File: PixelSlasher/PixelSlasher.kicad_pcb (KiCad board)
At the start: 2 copper layers, 52.8 x 123.6 mm, 16 parts, among them J1 VGA Input, Q1 BC337, Q2 BC337, Q3 BC337, U1 LM393, U2 LM393

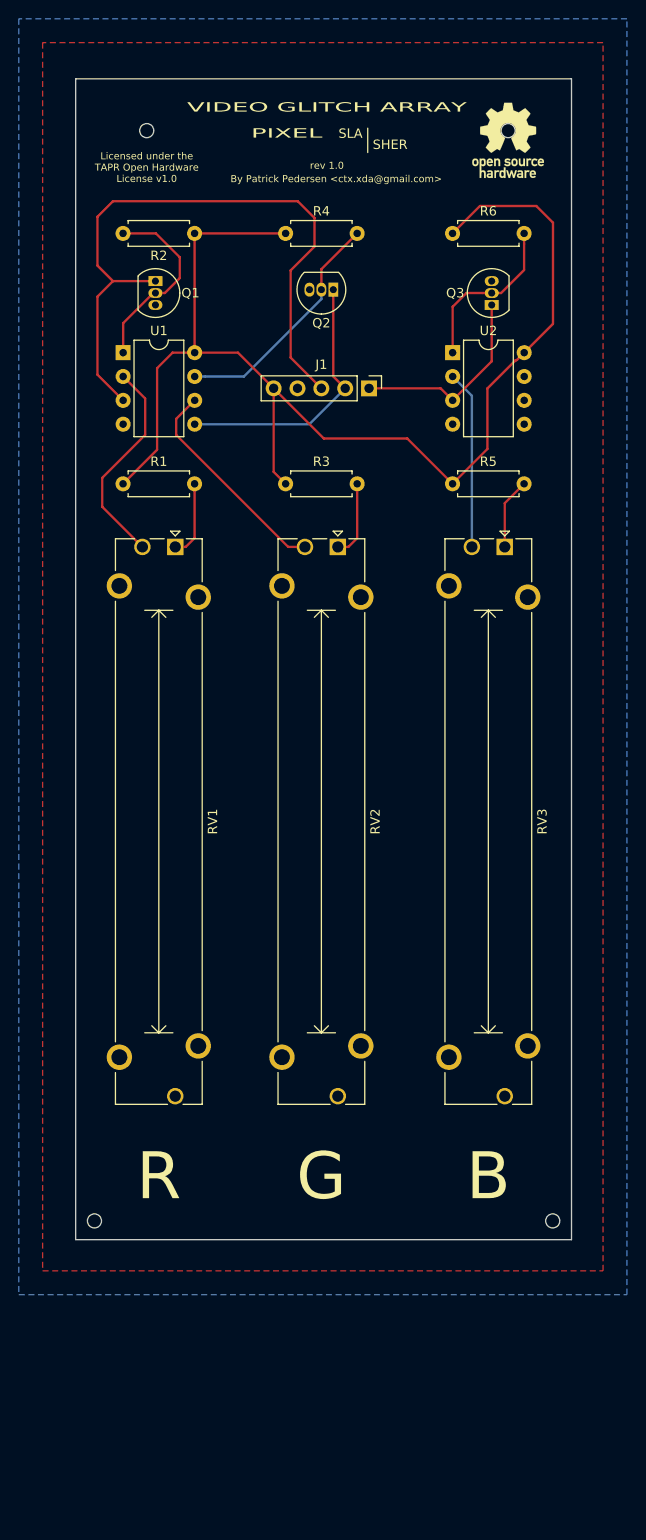
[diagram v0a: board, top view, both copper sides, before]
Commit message: Pixel Slasher: Rev 1.1: Inverted direction of slide pots
The previous configuration was counter-intuitive as we were decreasing
the number of artifacts as the slider went up.

Signed-off-by: Patrick Pedersen <ctx.xda@gmail.com>
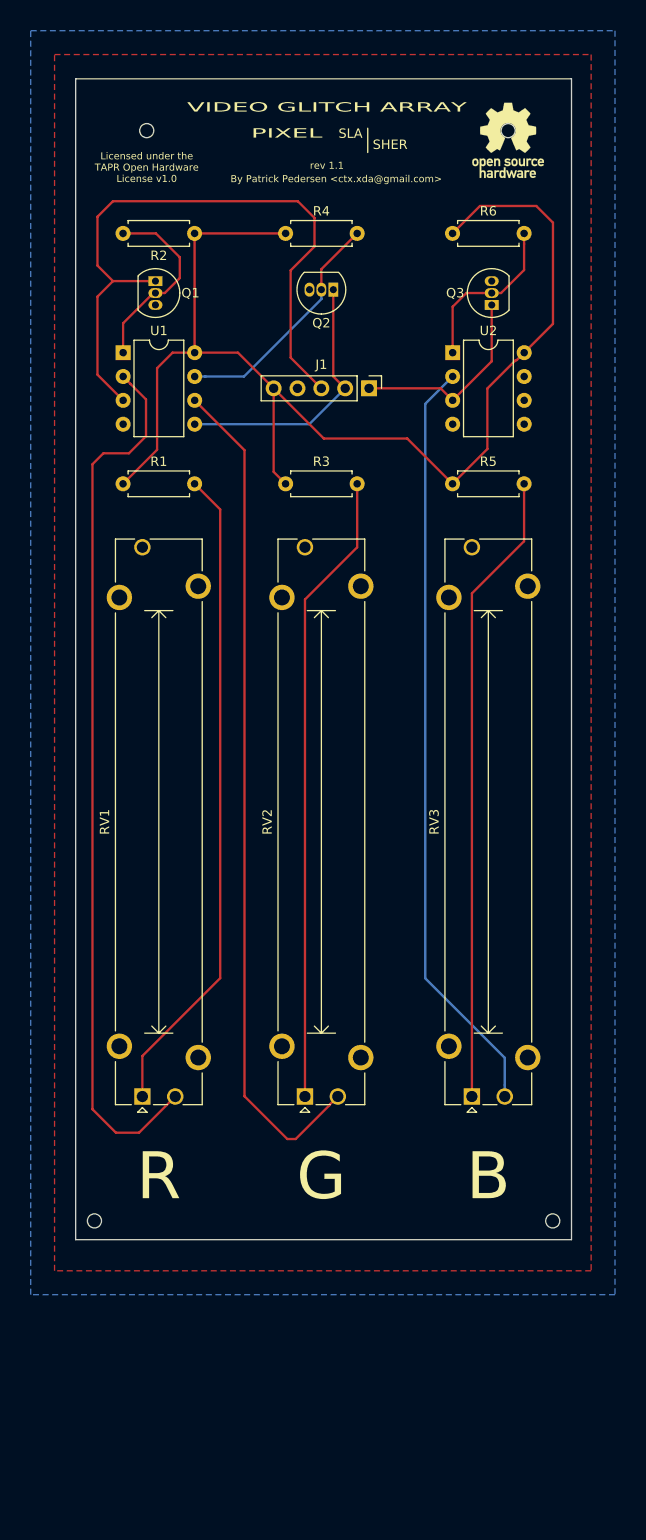
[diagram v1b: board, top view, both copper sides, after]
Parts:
- moved RV1 58.6 mm to (111.0, 141.5), turned to 90 degrees
- moved RV2 58.6 mm to (128.3, 141.5), turned to 90 degrees
- moved RV3 58.6 mm to (146.1, 141.5), turned to 90 degrees
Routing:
- net Net-(RV1-Pad2): track 22.8 -> 94.5 mm
- net Net-(RV2-Pad2): track 23.2 -> 90.0 mm
- net Net-(RV3-Pad2): track 19.0 -> 81.4 mm
- net Net-(R1-Pad2): track 8.23 -> 69.8 mm
- net Net-(R5-Pad2): track 7.57 -> 67.6 mm
- net Net-(R3-Pad2): track 8.23 -> 67.6 mm
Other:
- board text added: "rev 1.1"
- board text removed: "rev 1.0"

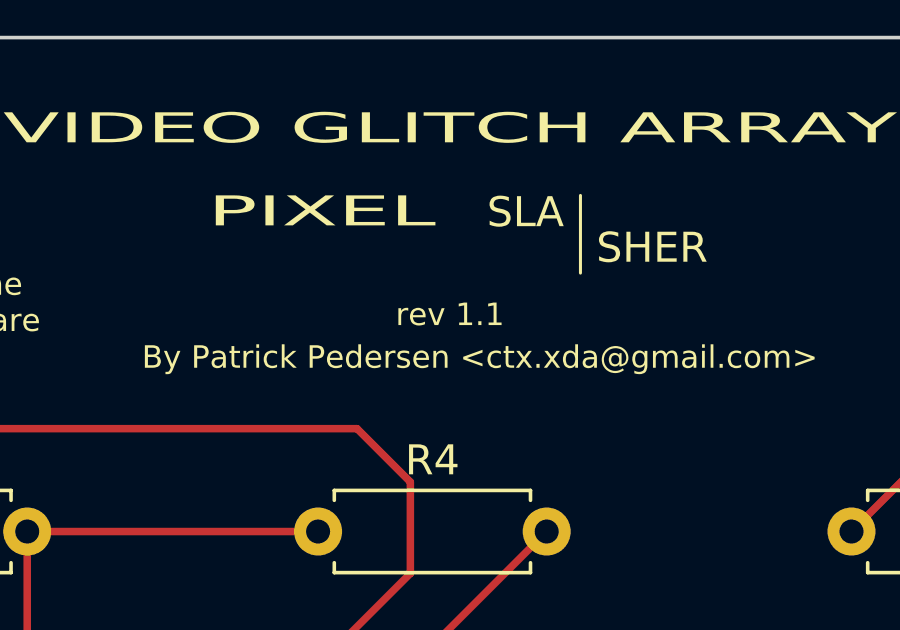
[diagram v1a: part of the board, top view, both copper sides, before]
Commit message: Updated PCB revisioning system to <SCHEM MAJOR>.<SCHEM MINOR>.<PCB>
Signed-off-by: Patrick Pedersen <ctx.xda@gmail.com>
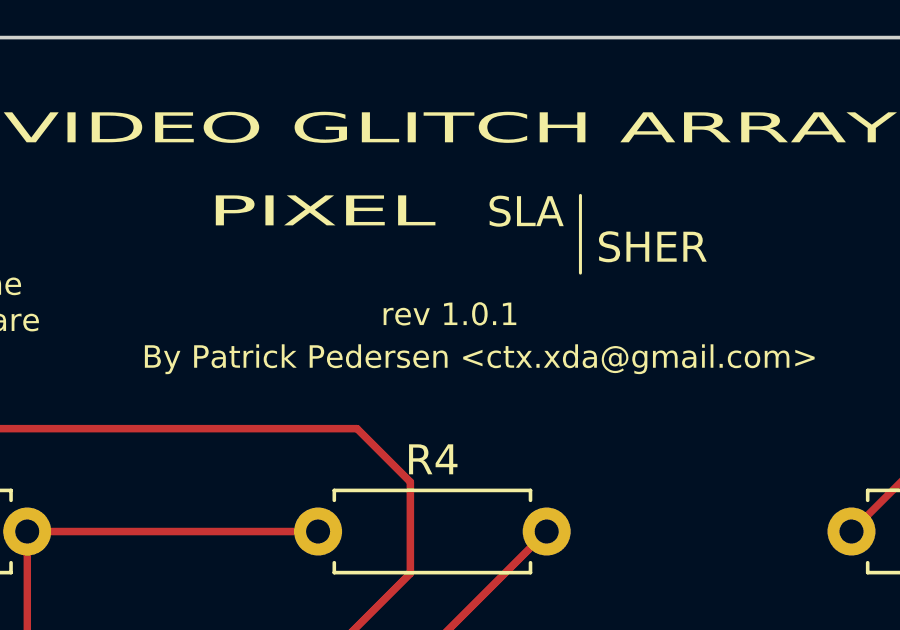
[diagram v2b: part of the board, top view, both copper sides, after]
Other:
- board text added: "rev 1.0.1"
- board text removed: "rev 1.1"
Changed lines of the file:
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@@
-(kicad_pcb (version 20171130) (host pcbnew 5.1.4-e60b266~84~ubuntu18.04.1)
+(kicad_pcb (version 20171130) (host pcbnew 5.1.4-e60b266~84~ubuntu19.04.1)
   (general
     (thickness 1.6)
@@
   (title_block
     (date 2019-08-30)
-    (rev 1.0)
+    (rev 1.0.1)
     (comment 2 https://www.tapr.org/ohl.html)
     (comment 3 "License: TAPR Open Hardware License v1.0")
@@
   (gr_circle (center 111.42 38.5826) (end 112.17 38.5826) (layer Edge.Cuts) (width 0.12))
   (gr_circle (center 149.9108 38.5826) (end 150.6608 38.5826) (layer Edge.Cuts) (width 0.12))
-  (gr_text "rev 1.1" (at 130.6068 42.30116) (layer F.SilkS)
+  (gr_text "rev 1.0.1" (at 130.6068 42.30116) (layer F.SilkS)
     (effects (font (size 0.75 0.75) (thickness 0.1)))
   )

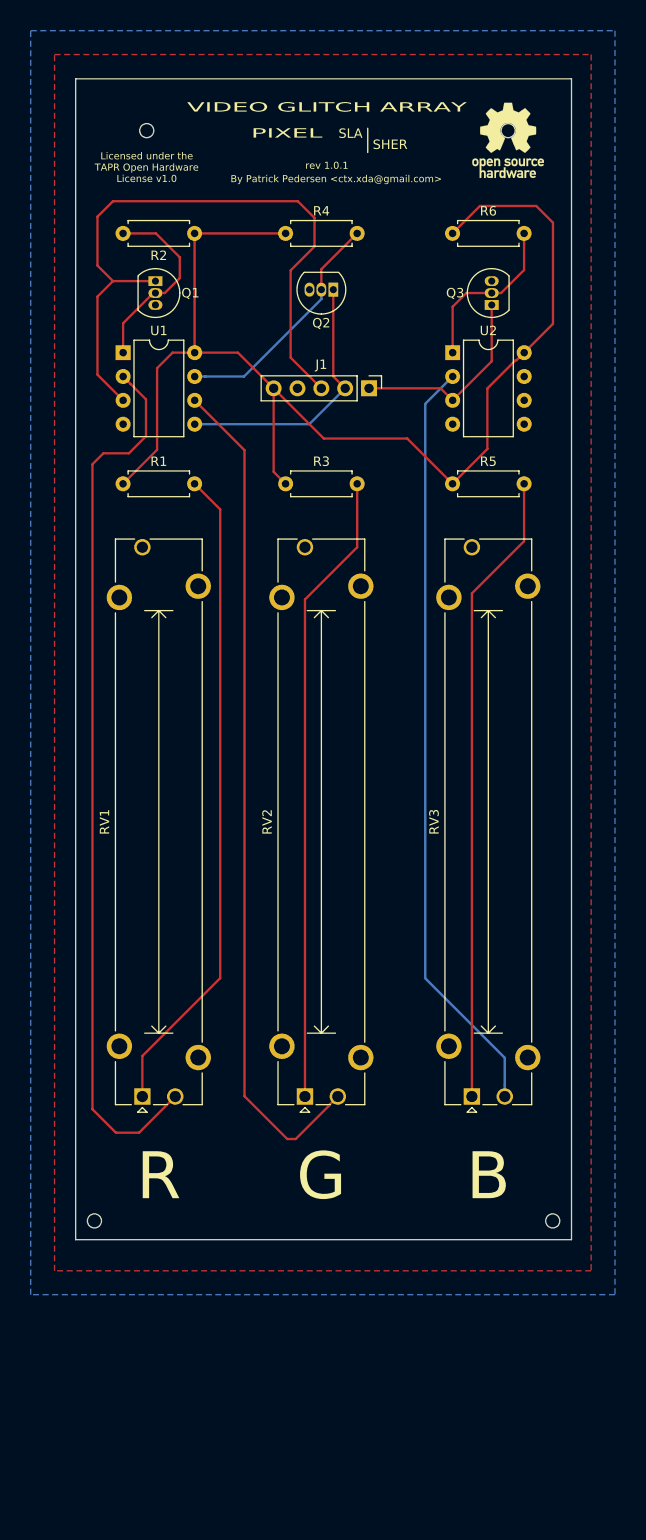
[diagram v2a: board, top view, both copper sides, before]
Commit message: Pixel Slasher: Rev 2.0.0: Added option for CV input
Signed-off-by: Patrick Pedersen <ctx.xda@gmail.com>
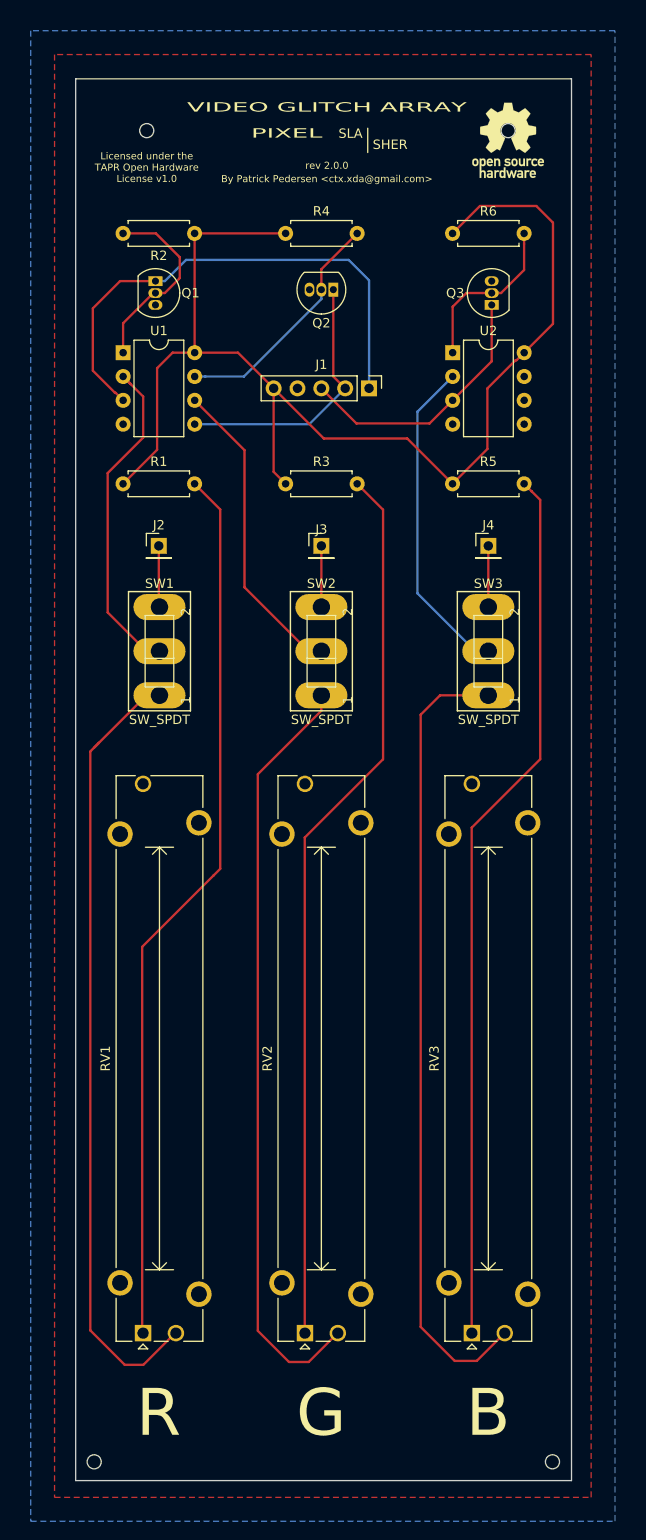
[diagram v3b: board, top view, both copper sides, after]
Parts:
- added J2: CV Red, Connector_PinHeader_2.54mm:PinHeader_1x01_P2.54mm_Vertical, F.Cu at (112.7, 82.8)
- added J3: CV Green, Connector_PinHeader_2.54mm:PinHeader_1x01_P2.54mm_Vertical, F.Cu at (130.0, 82.8)
- added J4: CV Blue, Connector_PinHeader_2.54mm:PinHeader_1x01_P2.54mm_Vertical, F.Cu at (147.8, 82.8)
- added SW1: SW_SPDT, SL19-121:255SB, F.Cu at (112.8, 94.0)
- added SW2: SW_SPDT, SL19-121:255SB, F.Cu at (130.0, 94.0)
- added SW3: SW_SPDT, SL19-121:255SB, F.Cu at (147.8, 94.0)
- moved RV1 25.2 mm to (111.0, 166.7)
- moved RV2 25.2 mm to (128.3, 166.7)
- moved RV3 25.2 mm to (146.1, 166.7)
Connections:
- Q1 pad 1: /VGA_B_IN -> /VGA_R_IN
- Q3 pad 1: /VGA_R_IN -> /VGA_B_IN
- U1 pad 2: Net-(RV1-Pad2) -> Net-(SW1-Pad2)
- U1 pad 3: /VGA_B_IN -> /VGA_R_IN
- U1 pad 6: Net-(RV2-Pad2) -> Net-(SW2-Pad2)
- U2 pad 2: Net-(RV3-Pad2) -> Net-(SW3-Pad2)
- U2 pad 3: /VGA_R_IN -> /VGA_B_IN
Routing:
- net /VGA_B_IN: track 71.7 -> 27.5 mm
- net Net-(SW1-Pad2): track 0.00 -> 35.9 mm
- net Net-(SW3-Pad2): track 0.00 -> 34.7 mm
- net /VGA_R_IN: track 21.3 -> 55.1 mm
- net Net-(SW2-Pad2): track 0.00 -> 33.1 mm
- net Net-(R3-Pad2): track 67.6 -> 95.1 mm
- net Net-(R5-Pad2): track 67.6 -> 94.2 mm
- net Net-(R1-Pad2): track 69.8 -> 95.0 mm
- net Net-(RV1-Pad2): track 94.5 -> 84.2 mm
- net Net-(RV2-Pad2): track 90.0 -> 81.6 mm
- net Net-(J2-Pad1): track 0.00 -> 6.55 mm
- net Net-(J4-Pad1): track 0.00 -> 6.52 mm
- net Net-(J3-Pad1): track 0.00 -> 6.52 mm
- net Net-(RV3-Pad2): track 81.4 -> 84.9 mm
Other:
- board size 52.8 x 123.6 mm -> 52.8 x 149.3 mm
- board text added: "rev 2.0.0"
- board text removed: "rev 1.0.1"

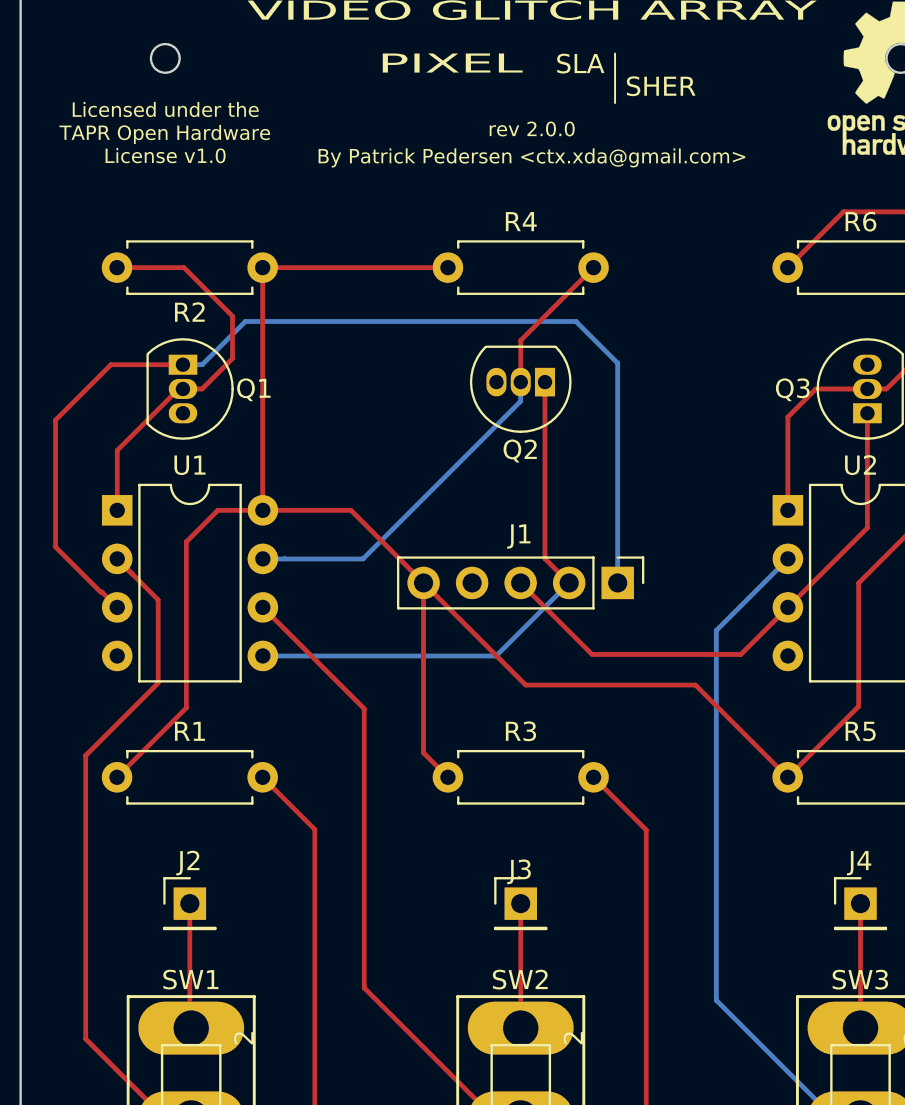
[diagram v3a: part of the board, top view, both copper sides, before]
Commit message: Pixel Slasher: rev 2.0.1: Re-oriented J1 to be more intuitive
Signed-off-by: Patrick Pedersen <ctx.xda@gmail.com>
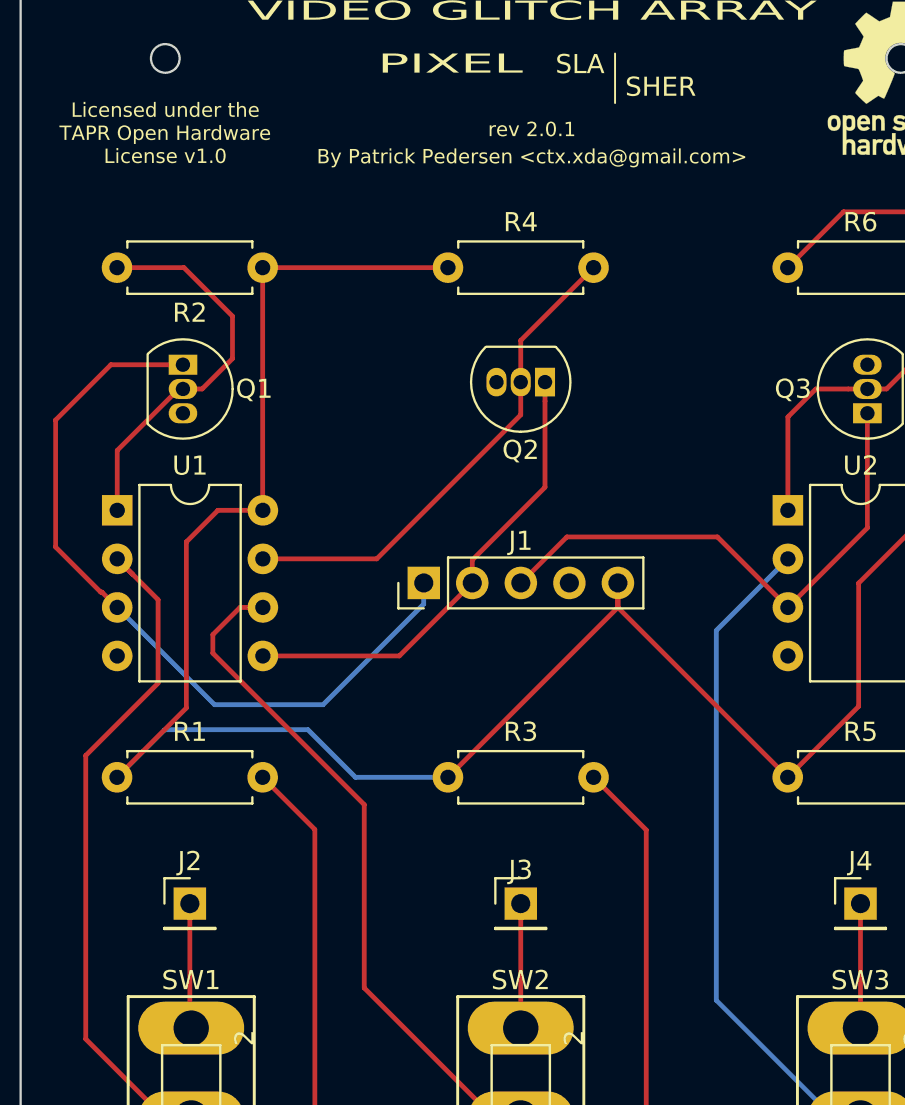
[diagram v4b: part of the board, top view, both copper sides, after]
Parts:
- moved J1 10.2 mm to (124.9, 66.0), turned to 90 degrees
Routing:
- net /VGA_R_IN: track 55.1 -> 40.5 mm
- net /VGA_G_IN: track 28.6 -> 24.6 mm
- net /VGA_5V_VCC_IN: track 129.8 -> 132.9 mm
- net Net-(SW2-Pad2): track 33.1 -> 36.0 mm
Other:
- board text added: "rev 2.0.1"
- board text removed: "rev 2.0.0"
